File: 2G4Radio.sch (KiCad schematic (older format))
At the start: 21 parts

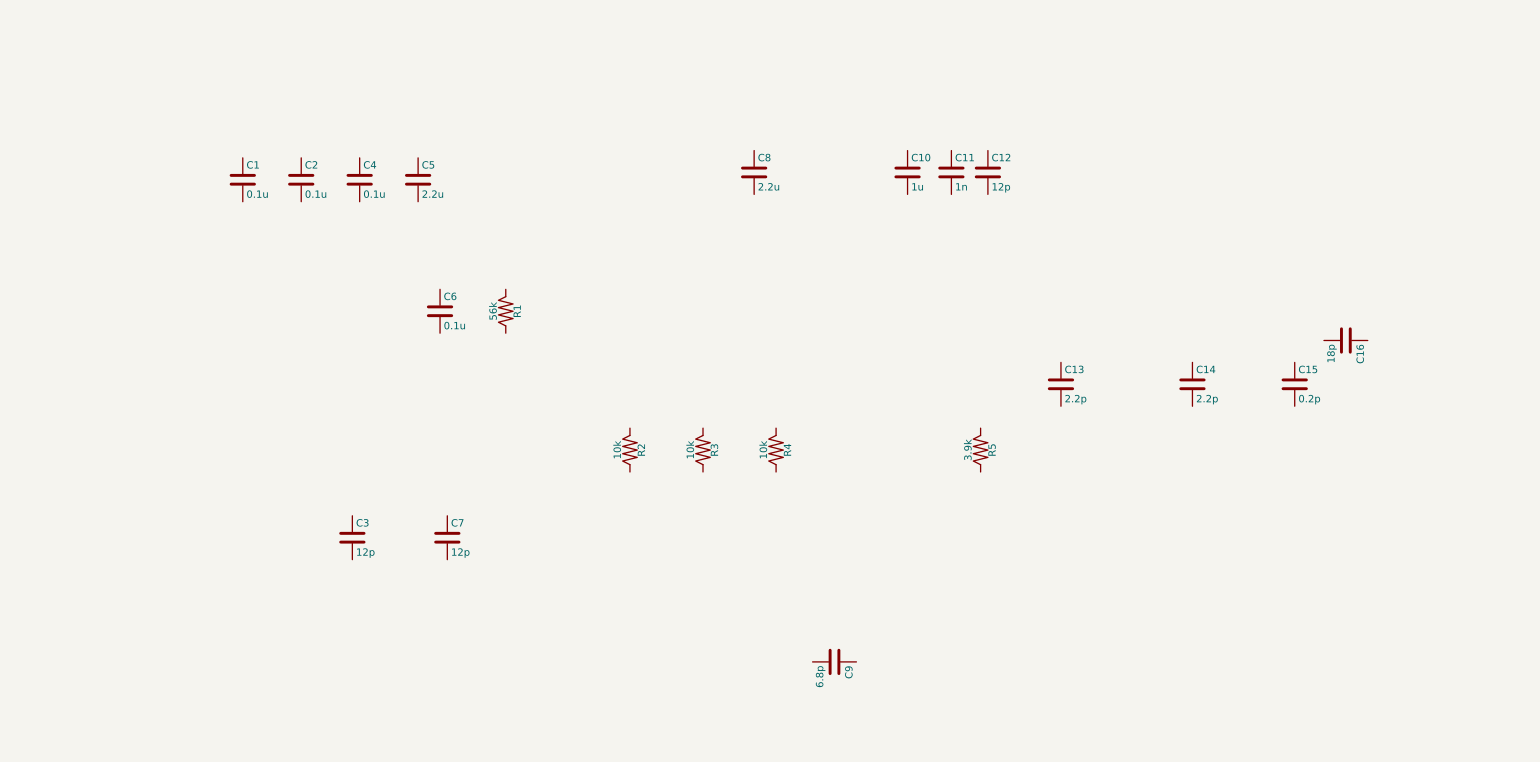
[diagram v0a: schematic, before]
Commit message: added some radio components.
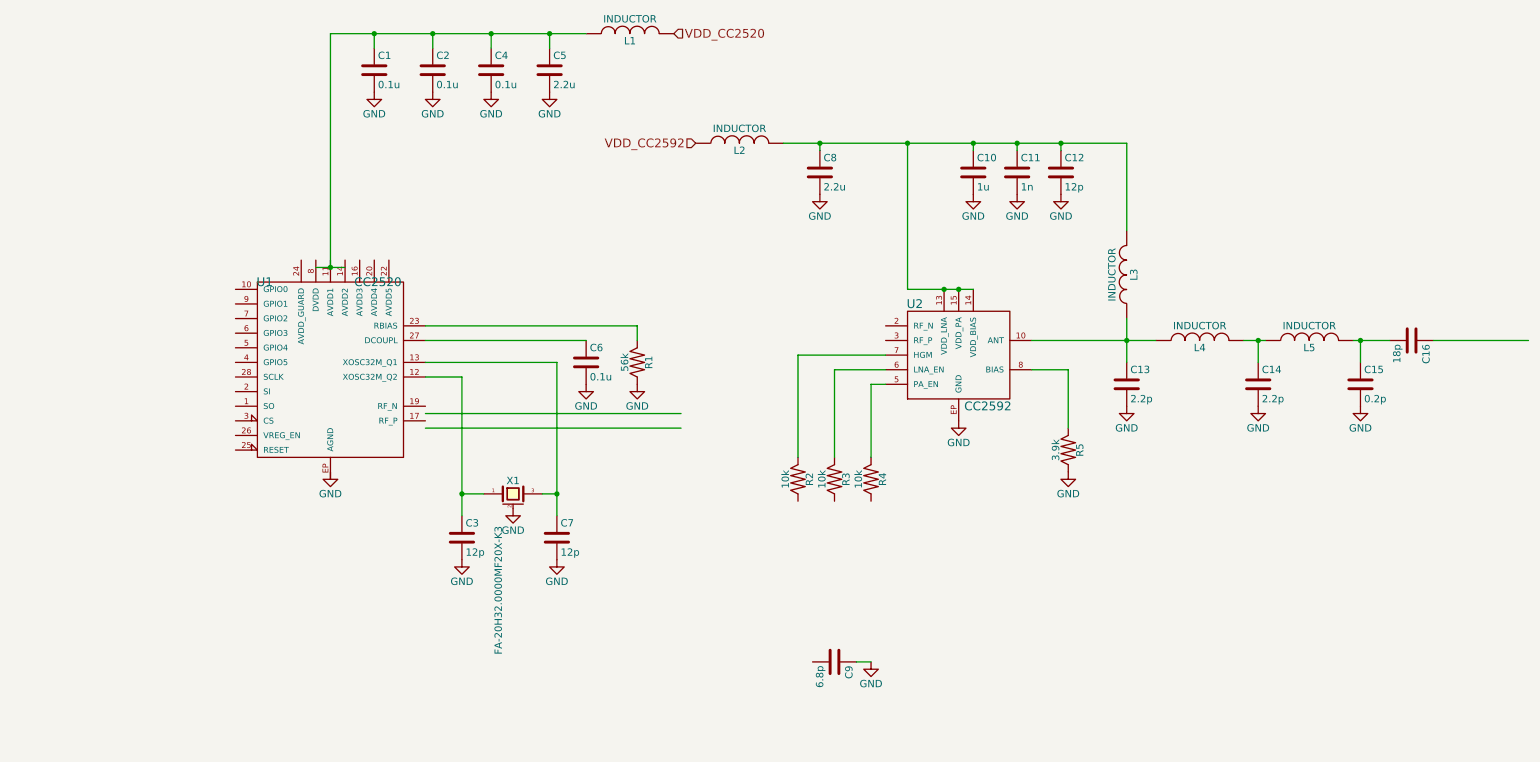
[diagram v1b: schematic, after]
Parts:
- added L1, L2, L3, L4, L5: INDUCTOR, Resistors_SMD:R_0402, symbol INDUCTOR
- added U1: CC2520, SMD_Packages:RHD_S-PVQFN-N28, symbol CC2520
- added U2: CC2592, SMD_Packages:RGV_S-PVQFN-N16, symbol CC2592
- added X1: FA-20H32.0000MF20X-K3, symbol CRYSTAL_SMD
- C1, C10, C11, C12, C13, C14, C15, C16, C2, C3, C4, C5, C6, C7, C8, C9: footprint Passives:C_0402 -> Capacitors_SMD:C_0402
- R1, R2, R3, R4, R5: footprint Passives:R_0402 -> Resistors_SMD:R_0402
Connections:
- net labels added: GND, VDD_CC2520, VDD_CC2592
- wire segments 0 -> 42
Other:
- moved on the sheet: C1, C10, C11, C12, C13, C14, C15, C16, C2, C3, C4, C5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

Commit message: Added more RF components
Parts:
- added R6: R3-RH, Resistors_SMD:R3_RH_0402, symbol R3-RH
- added R7: R3-LH, Resistors_SMD:R3_LH_0402, symbol R3-LH
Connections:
- wire segments 42 -> 48
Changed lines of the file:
@@
 Wire Wire Line
 	5850 3550 6450 3550
+$Comp
+L R3-LH R7
+U 1 1 559B6ED9
+P 5250 4050
+F 0 "R7" H 5200 4150 50  0000 C CNN
+F 1 "R3-LH" V 5500 4200 50  0000 C CNN
+F 2 "Resistors_SMD:R3_LH_0402" H 5250 3980 30  0001 C CNN
+F 3 "" V 5250 4050 30  0000 C CNN
+	1    5250 4050
+	-1   0    0    1
+$EndComp
+$Comp
+L R3-RH R6
+U 1 1 559B7240
+P 5250 3950
+F 0 "R6" H 5150 3850 50  0000 C CNN
+F 1 "R3-RH" V 5500 3800 50  0000 C CNN
+F 2 "Resistors_SMD:R3_RH_0402" H 5250 3880 30  0001 C CNN
+F 3 "" V 5250 3950 30  0000 C CNN
+	1    5250 3950
+	-1   0    0    1
+$EndComp
+Wire Wire Line
+	5400 3950 5550 3950
+Wire Wire Line
+	5550 3950 5550 3350
+Wire Wire Line
+	5550 3350 6450 3350
+Wire Wire Line
+	5400 4050 5650 4050
+Wire Wire Line
+	5650 4050 5650 3450
+Wire Wire Line
+	5650 3450 6450 3450
 $EndSCHEMATC

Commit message: Added baluns
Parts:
- added U5: LDB182G4520C-110, SMD_Packages:LDB18, symbol LDB182G4520C-110
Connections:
- wire segments 48 -> 55
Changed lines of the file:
@@
 Wire Wire Line
 	5650 3450 6450 3450
+$Comp
+L LDB182G4520C-110 U5
+U 1 1 559C9F2F
+P 5550 5750
+F 0 "U5" H 5350 5950 60  0000 C CNN
+F 1 "LDB182G4520C-110" H 5750 5550 60  0000 C CNN
+F 2 "SMD_Packages:LDB18" H 5550 5750 60  0001 C CNN
+F 3 "" H 5550 5750 60  0000 C CNN
+	1    5550 5750
+	1    0    0    -1
+$EndComp
+Wire Wire Line
+	5150 5650 5100 5650
+Wire Wire Line
+	5100 5650 5100 4350
+Wire Wire Line
+	5150 5850 4900 5850
+Wire Wire Line
+	4900 5850 4900 3600
+Wire Wire Line
+	4900 3600 5100 3600
+Wire Wire Line
+	5100 3600 5100 3650
+Wire Wire Line
+	5950 5850 7100 5850
 $EndSCHEMATC

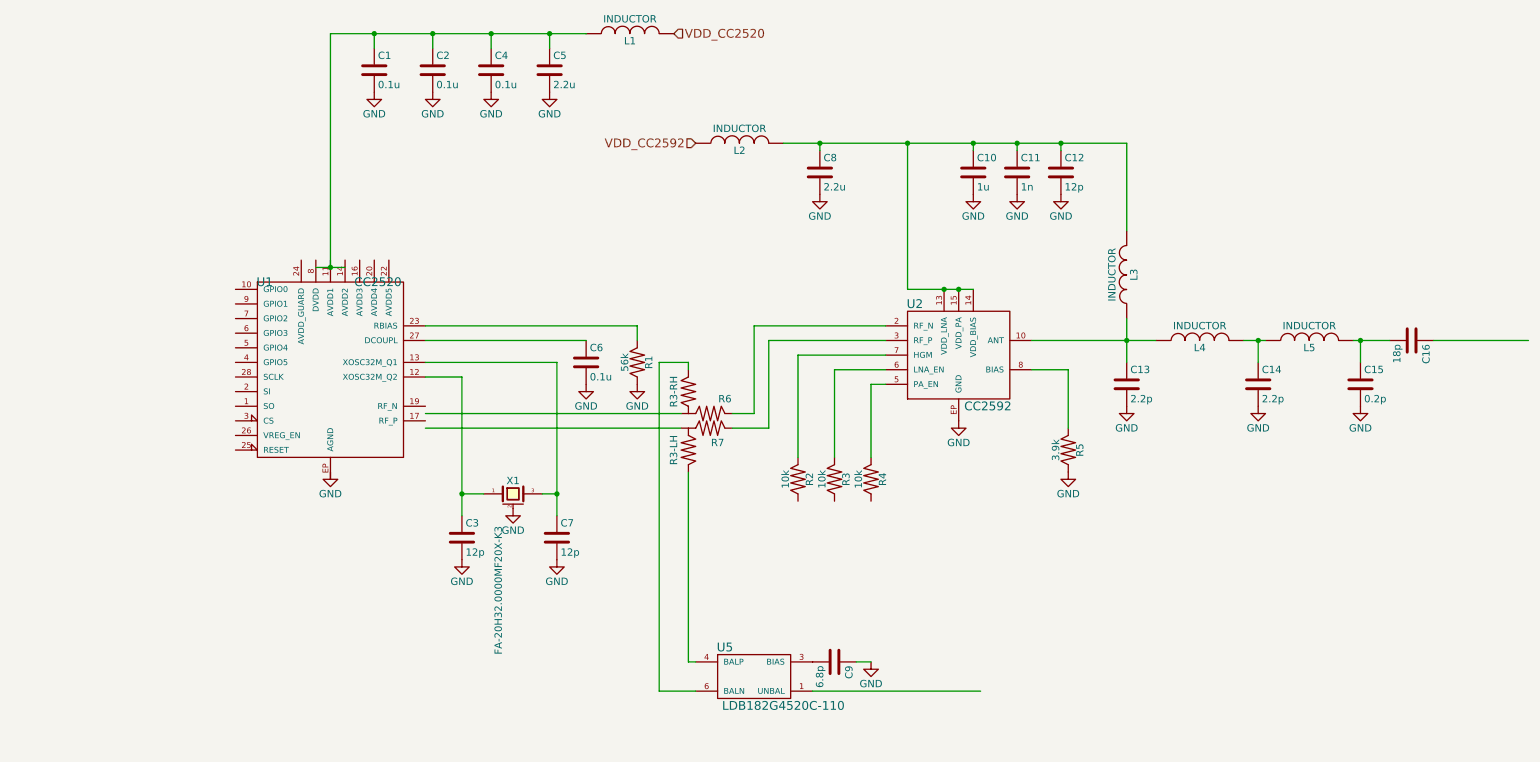
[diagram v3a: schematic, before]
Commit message: Finished schematic of 2.4GHz and 900MHz radios
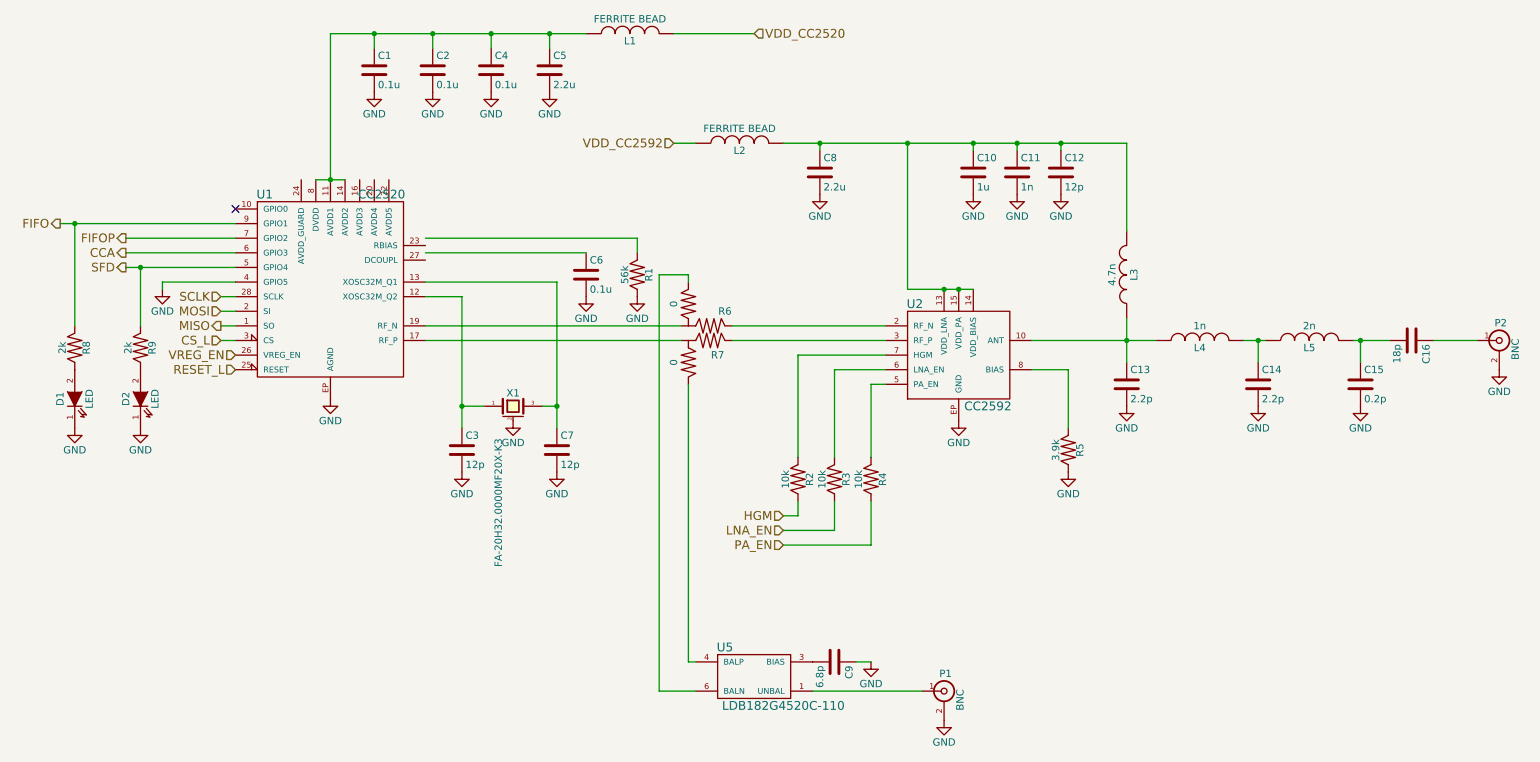
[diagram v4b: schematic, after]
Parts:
- added D1, D2: LED, LEDs:LED-0603, symbol LED
- added P1, P2: BNC, Connect:SMB_Straight, symbol BNC
- added R8, R9: 2k, Resistors_SMD:R_0402, symbol R
- L1, L2: value INDUCTOR -> FERRITE BEAD
- L3: value INDUCTOR -> 4.7n
- L4: value INDUCTOR -> 1n
- L5: value INDUCTOR -> 2n
- R6: value R3-RH -> 0
- R7: value R3-LH -> 0
- X1: footprint (none) -> Crystals_Oscillators_SMD:FA-20H
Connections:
- net labels added: CCA, CS_L, FIFO, FIFOP, HGM, LNA_EN, MISO, MOSI, PA_EN, RESET_L, SCLK, SFD, VREG_EN
- wire segments 55 -> 72
- no-connect marks 0 -> 1
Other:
- moved on the sheet: C3, C6, C7, R1, R6, R7, U1, X1

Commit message: Updated layout
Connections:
- net at U1.17 (RF_P): now also R6.1; no longer R7.2
- net at U1.19 (RF_N): now also R7.1; no longer R6.2
- net at U2.2 (RF_N): now also R7.2; no longer R6.1
- net at U2.3 (RF_P): now also R6.2; no longer R7.1
- net at R7.3: now also U5.6 (BALN); no longer U5.4 (BALP)
- net at R6.3: now also U5.4 (BALP); no longer U5.6 (BALN)
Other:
- moved on the sheet: R6, R7
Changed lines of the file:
@@
 L R3-LH R7
 U 1 1 559B6ED9
-P 5250 3450
-F 0 "R7" H 5200 3550 50  0000 C CNN
-F 1 "0" V 5500 3600 50  0000 C CNN
-F 2 "Resistors_SMD:R3_LH_0402" H 5250 3380 30  0001 C CNN
-F 3 "" V 5250 3450 30  0000 C CNN
-	1    5250 3450
-	-1   0    0    1
+P 5200 3350
+F 0 "R7" H 5150 3450 50  0000 C CNN
+F 1 "0" V 5450 3500 50  0000 C CNN
+F 2 "Resistors_SMD:R3_LH_0402" H 5200 3280 30  0001 C CNN
+F 3 "" V 5200 3350 30  0000 C CNN
+	1    5200 3350
+	1    0    0    -1
 $EndComp
 $Comp
 L R3-RH R6
 U 1 1 559B7240
-P 5250 3350
-F 0 "R6" H 5150 3250 50  0000 C CNN
-F 1 "0" V 5500 3200 50  0000 C CNN
-F 2 "Resistors_SMD:R3_RH_0402" H 5250 3280 30  0001 C CNN
-F 3 "" V 5250 3350 30  0000 C CNN
-	1    5250 3350
-	-1   0    0    1
+P 5200 3450
+F 0 "R6" H 5100 3350 50  0000 C CNN
+F 1 "0" V 5450 3300 50  0000 C CNN
+F 2 "Resistors_SMD:R3_RH_0402" H 5200 3380 30  0001 C CNN
+F 3 "" V 5200 3450 30  0000 C CNN
+	1    5200 3450
+	1    0    0    -1
 $EndComp
 $Comp
@@
 	4900 3000 4900 5850
 Wire Wire Line
-	4900 3000 5100 3000
-Wire Wire Line
-	5100 3000 5100 3050
+	4900 3000 5350 3000
 Wire Wire Line
 	5950 5850 6700 5850
@@
 Wire Wire Line
 	1500 3050 1500 3100
+Wire Wire Line
+	5100 3750 5350 3750
+Wire Wire Line
+	5350 3000 5350 3050
 $EndSCHEMATC
